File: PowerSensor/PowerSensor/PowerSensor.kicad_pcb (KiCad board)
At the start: 2 copper layers, 35.6 x 22.6 mm, 14 parts, among them J1 Current Sens, J3 BAT+, J4 BAT-, J5 Screw_Terminal_01x04, U1 ACS712ELCTR-20A-T_NRND

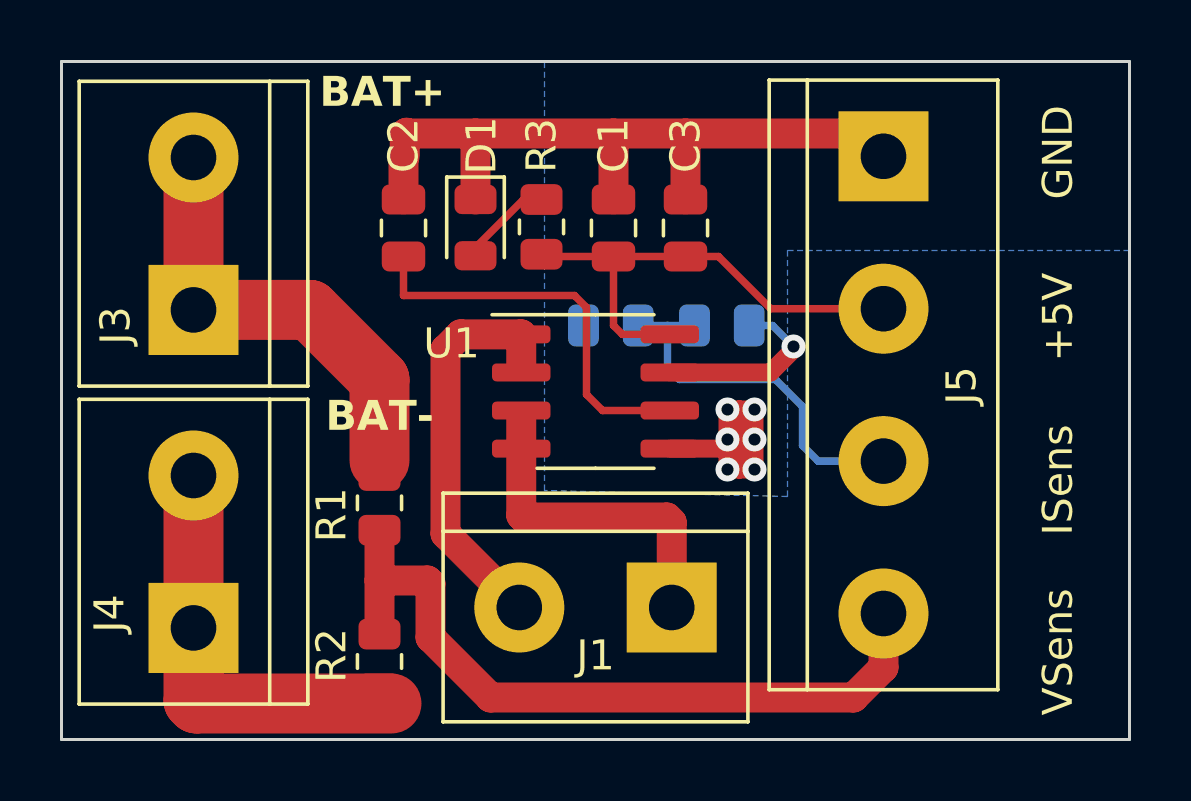
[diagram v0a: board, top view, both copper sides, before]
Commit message: Optimize the routig on PCB
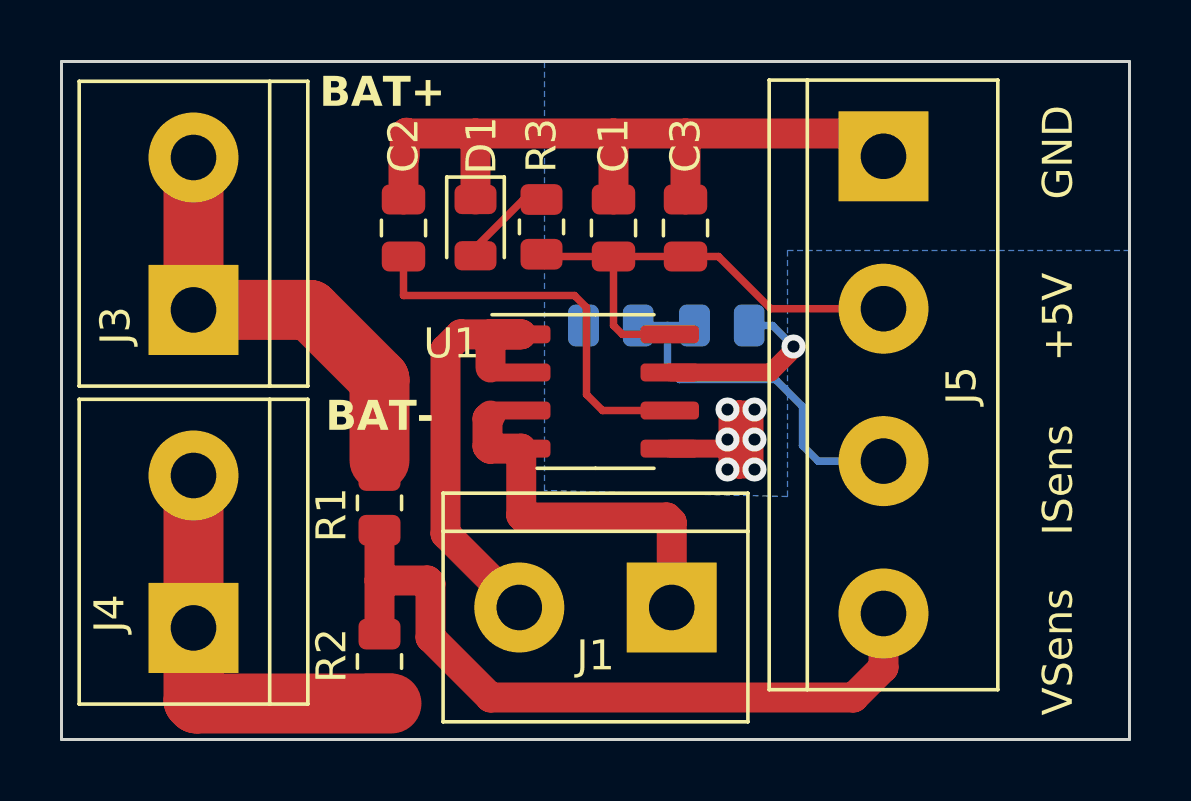
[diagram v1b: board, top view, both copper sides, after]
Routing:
- net IN-: track 11.2 -> 12.4 mm
- net IN+: track 13.4 -> 14.5 mm
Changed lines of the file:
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@@
   (segment (start 105.2 87.4) (end 105.2 87.675) (width 0.25) (layer "F.Cu") (net 2))
   (segment (start 106.8 85.8) (end 105.2 87.4) (width 0.25) (layer "F.Cu") (net 2))
+  (segment (start 105.6 94.025) (end 105.6 93.1) (width 1) (layer "F.Cu") (net 3))
+  (segment (start 105.68 94.105) (end 105.6 94.025) (width 1) (layer "F.Cu") (net 3))
   (segment (start 111.74 99.12) (end 111.74 96.56) (width 1) (layer "F.Cu") (net 3))
+  (segment (start 105.6 93.1) (end 105.7 93) (width 1) (layer "F.Cu") (net 3))
   (segment (start 111.74 99.4) (end 111.74 99.12) (width 0.2) (layer "F.Cu") (net 3))
   (segment (start 111.74 96.56) (end 111.58 96.4) (width 1) (layer "F.Cu") (net 3))
+  (segment (start 106.725 94.105) (end 105.68 94.105) (width 1) (layer "F.Cu") (net 3))
   (segment (start 106.725 96.325) (end 106.725 94.105) (width 1) (layer "F.Cu") (net 3))
-  (segment (start 106.725 94.105) (end 106.725 93.1) (width 1) (layer "F.Cu") (net 3))
   (segment (start 106.8 96.4) (end 106.725 96.325) (width 1) (layer "F.Cu") (net 3))
   (segment (start 111.58 96.4) (end 106.8 96.4) (width 1) (layer "F.Cu") (net 3))
@@
   (segment (start 104.2 90.8) (end 104.705 90.295) (width 1) (layer "F.Cu") (net 4))
   (segment (start 104.2 96.94) (end 104.2 90.8) (width 1) (layer "F.Cu") (net 4))
-  (segment (start 106.725 90.295) (end 106.725 91.3) (width 1) (layer "F.Cu") (net 4))
+  (segment (start 106.725 90.295) (end 105.7 90.295) (width 1) (layer "F.Cu") (net 4))
+  (segment (start 105.7 90.295) (end 105.7 91.4) (width 1) (layer "F.Cu") (net 4))
   (segment (start 95.9 102.6) (end 95.8 102.5) (width 2) (layer "F.Cu") (net 5))
   (segment (start 102.4 102.6) (end 95.9 102.6) (width 2) (layer "F.Cu") (net 5))
